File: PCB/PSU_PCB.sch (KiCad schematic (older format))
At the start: 130 parts, among them CON1 BARREL_JACK, IC1 ATMEGA328-P, P1 USB_OTG, P2 FTDI, P3 V+, P4 V-, P5 ISP, P6 I2C, P7 LCD_Display, Q1 TIP32CG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

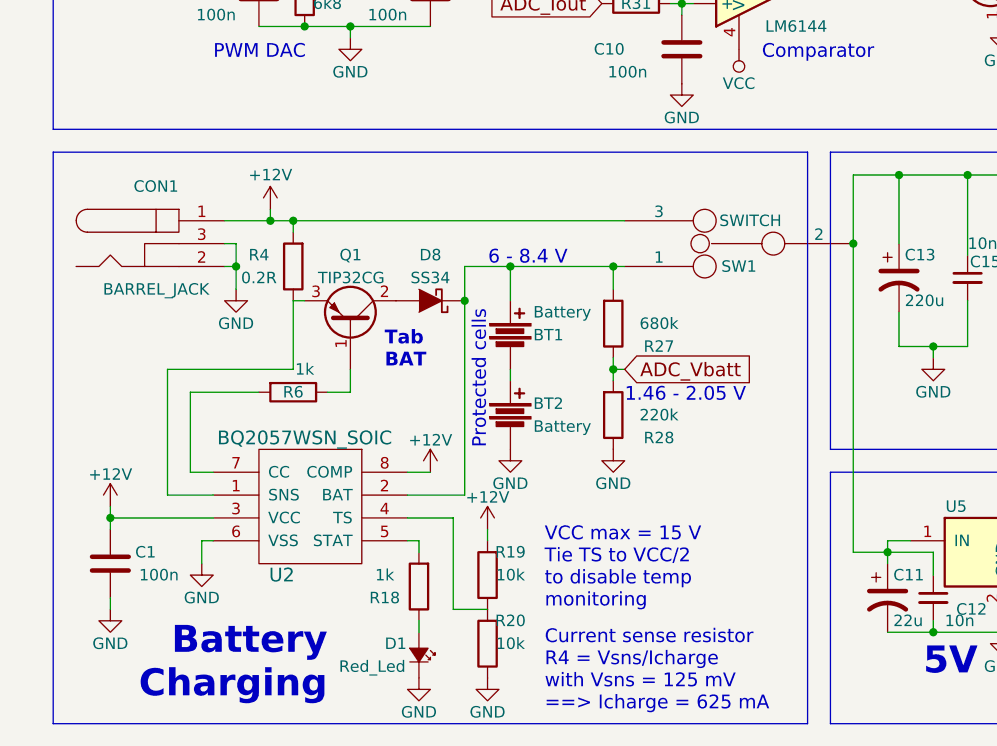
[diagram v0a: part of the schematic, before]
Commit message: Added protection resistor to charging circuitry
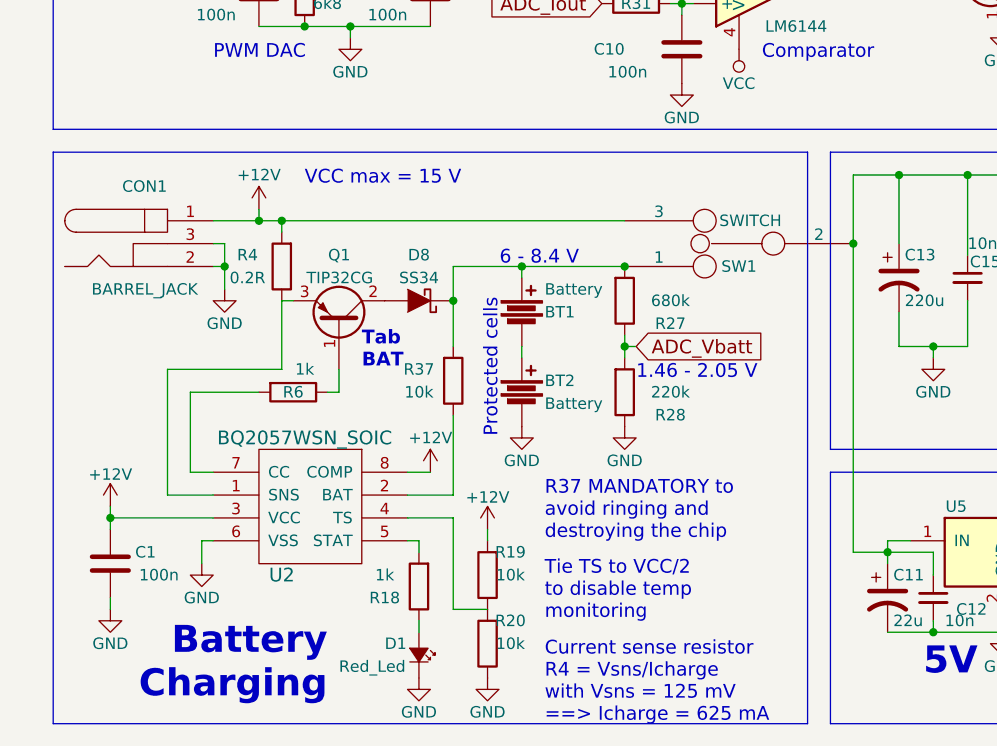
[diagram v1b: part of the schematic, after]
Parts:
- added R37: 10k, Resistors_ThroughHole:R_Axial_DIN0207_L6.3mm_D2.5mm_P10.16mm_Horizontal, symbol R
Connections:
- net at BT1.1, D8.1 (K), R27.2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: now also R37.2; no longer U2.2 (BAT)
- new net: R37.1, U2.2 (BAT)
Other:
- note added: "R37 MANDATORY to \navoid ringing and\ndestroying the chip"
- note added: "Tie TS to VCC/2 \nto disable temp \nmonitoring"
- note added: "VCC max = 15 V"
- note removed: "VCC max = 15 V\nTie TS to VCC/2 \nto disable temp \nmonitoring"
- moved on the sheet: BT1, BT2, CON1, D8, Q1, R27, R28, R4

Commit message: Small BOM optimisation
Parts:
- C17, C8: value 2u2 -> 22u
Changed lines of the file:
@@
 P 4800 1550
 F 0 "C17" H 4550 1550 50  0000 L CNN
-F 1 "2u2" H 4550 1450 50  0000 L CNN
+F 1 "22u" H 4550 1450 50  0000 L CNN
 F 2 "Capacitors_ThroughHole:C_Radial_D10_L13_P5" H 4800 1550 50  0001 C CNN
 F 3 "" H 4800 1550 50  0000 C CNN
@@
 P 2800 1200
 F 0 "C8" H 2550 1200 50  0000 L CNN
-F 1 "2u2" H 2550 1100 50  0000 L CNN
+F 1 "22u" H 2550 1100 50  0000 L CNN
 F 2 "Capacitors_ThroughHole:C_Radial_D10_L13_P5" H 2800 1200 50  0001 C CNN
 F 3 "" H 2800 1200 50  0000 C CNN
@@
 8E D2 4E 06 E9 83 31 0C B8 01 D4 62 7A FA FE CA 1E E7 AB A8 50 4D B8 D1 52 86 A6 EF 44 4C F7 6B
 69 A6 CB 4C 71 E1 73 B8 2B 4F 00 E7 75 28 F9 2E A2 C6 63 AC 40 DB 07 B2 19 61 39 9A 3C 4A F1 B4
-F5 AD 2E B3 0D FC 7F 6D 80 3F 3C 28 70 B1 D5 00 00 00 00 49 45 4E 44 AE 42 60 82 D9
+F5 AD 2E B3 0D FC 7F 6D 80 3F 3C 28 70 B1 D5 00 00 00 00 49 45 4E 44 AE 42 60 82 0E
 EndData
 $EndBitmap
@@
 00 09 E8 04 41 10 04 61 00 48 40 27 08 82 20 08 03 40 02 3A 41 10 04 41 18 00 23 00 F5 5D DD 09
 82 20 08 82 20 B4 52 CF 06 60 0D 60 1C 9A D7 A4 13 04 41 10 04 D1 BD 50 00 7E F8 7F 36 C9 A5 48
-A4 FE A8 58 00 00 00 00 49 45 4E 44 AE 42 60 82 A0
+A4 FE A8 58 00 00 00 00 49 45 4E 44 AE 42 60 82 90
 EndData
 $EndBitmap
